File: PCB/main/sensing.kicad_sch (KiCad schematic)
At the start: 11 parts

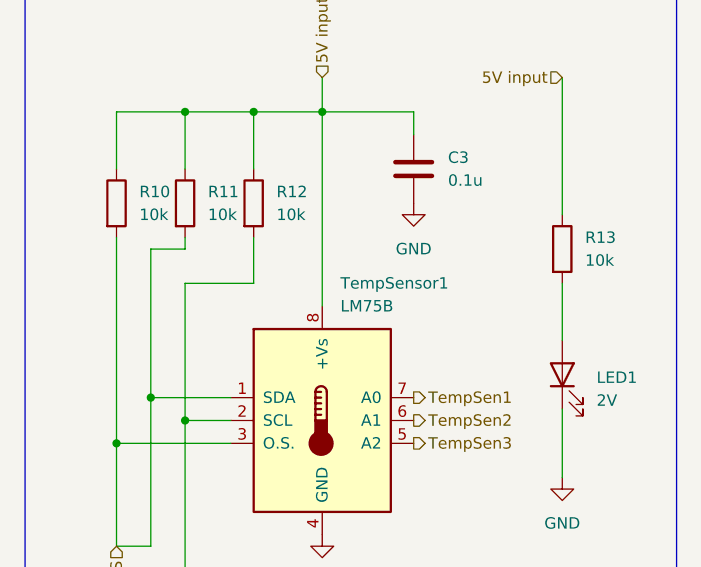
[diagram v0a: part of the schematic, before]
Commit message: rewired PCB and changed relevant footprints. production files regenerated
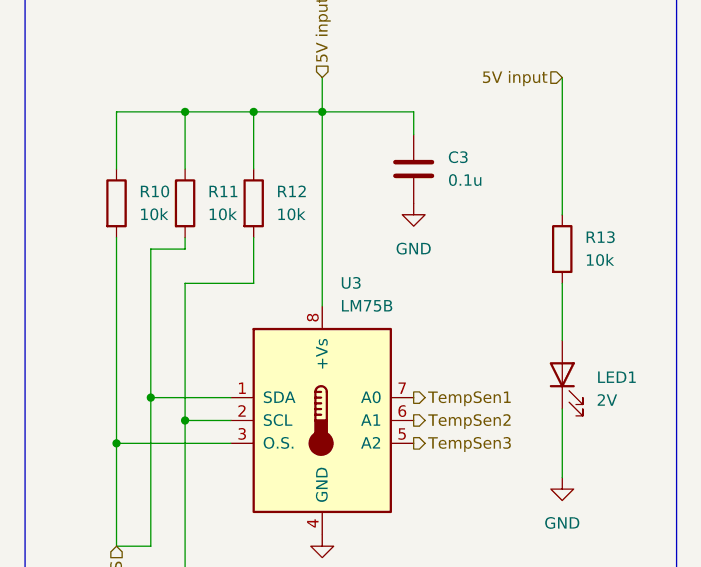
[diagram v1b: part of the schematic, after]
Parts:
- LDR1, LDR2: footprint Resistor_SMD:R_0201_0603Metric -> Resistor_THT:R_Axial_DIN0204_L3.6mm_D1.6mm_P1.90mm_Vertical
- R10, R11, R12, R13, R8, R9: footprint Resistor_SMD:R_0201_0603Metric -> Resistor_SMD:R_0603_1608Metric
- U3: renamed from TempSensor1; footprint Package_SO:MSOP-8_3x3mm_P0.65mm -> LM75BD:SOIC127P600X175-8N; LCSC C2837470 -> C34565; Price 0.4002 -> C34565
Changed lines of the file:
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@@
       (effects (font (size 1.27 1.27)) (justify left))
     )
-    (property "Footprint" "Resistor_SMD:R_0201_0603Metric" (id 2) (at 235.712 113.03 90)
+    (property "Footprint" "Resistor_SMD:R_0603_1608Metric" (id 2) (at 235.712 113.03 90)
       (effects (font (size 1.27 1.27)) hide)
     )
@@
       (effects (font (size 1.27 1.27)) (justify left))
     )
-    (property "Footprint" "Resistor_SMD:R_0201_0603Metric" (id 2) (at 153.67 99.06 0)
+    (property "Footprint" "Resistor_SMD:R_0603_1608Metric" (id 2) (at 153.67 99.06 0)
       (effects (font (size 1.27 1.27)) (justify left) hide)
     )
@@
       (effects (font (size 1.27 1.27)) (justify left))
     )
-    (property "Footprint" "Resistor_SMD:R_0201_0603Metric" (id 2) (at 220.472 113.03 90)
+    (property "Footprint" "Resistor_SMD:R_0603_1608Metric" (id 2) (at 220.472 113.03 90)
       (effects (font (size 1.27 1.27)) hide)
     )
@@
       (effects (font (size 1.27 1.27)) (justify left))
     )
-    (property "Footprint" "Resistor_SMD:R_0201_0603Metric" (id 2) (at 270.002 118.11 90)
+    (property "Footprint" "Resistor_SMD:R_0603_1608Metric" (id 2) (at 270.002 118.11 90)
       (effects (font (size 1.27 1.27)) hide)
     )
@@
       (effects (font (size 1.27 1.27)) (justify left))
     )
-    (property "Footprint" "Resistor_SMD:R_0201_0603Metric" (id 2) (at 128.27 140.97 90)
+    (property "Footprint" "Resistor_THT:R_Axial_DIN0204_L3.6mm_D1.6mm_P1.90mm_Vertical" (id 2) (at 128.27 140.97 90)
       (effects (font (size 1.27 1.27)) (justify left) hide)
     )
@@
       (effects (font (size 1.27 1.27)) (justify left))
     )
-    (property "Footprint" "Resistor_SMD:R_0201_0603Metric" (id 2) (at 100.33 105.41 0)
+    (property "Footprint" "Resistor_SMD:R_0603_1608Metric" (id 2) (at 100.33 105.41 0)
       (effects (font (size 1.27 1.27)) (justify left) hide)
     )
@@
       (effects (font (size 1.27 1.27)) (justify left))
     )
-    (property "Footprint" "Resistor_SMD:R_0201_0603Metric" (id 2) (at 228.092 113.03 90)
+    (property "Footprint" "Resistor_SMD:R_0603_1608Metric" (id 2) (at 228.092 113.03 90)
       (effects (font (size 1.27 1.27)) hide)
     )
@@
   (symbol (lib_id "Sensor_Temperature:LM75B") (at 245.11 137.16 0) (unit 1)
     (in_bom yes) (on_board yes) (fields_autoplaced)
-    (property "Reference" "TempSensor1" (id 0) (at 247.1294 121.92 0)
+    (property "Reference" "U3" (id 0) (at 247.1294 121.92 0)
       (effects (font (size 1.27 1.27)) (justify left))
     )
@@
       (effects (font (size 1.27 1.27)) (justify left))
     )
-    (property "Footprint" "Package_SO:MSOP-8_3x3mm_P0.65mm" (id 2) (at 245.11 137.16 0)
+    (property "Footprint" "LM75BD:SOIC127P600X175-8N" (id 2) (at 245.11 137.16 0)
       (effects (font (size 1.27 1.27)) hide)
     )
@@
       (effects (font (size 1.27 1.27)) hide)
     )
-    (property "LCSC" "C2837470" (id 4) (at 245.11 137.16 0)
-      (effects (font (size 1.27 1.27)) hide)
-    )
-    (property "Price" "0.4002" (id 5) (at 245.11 137.16 0)
+    (property "LCSC" "C34565" (id 4) (at 245.11 137.16 0)
+      (effects (font (size 1.27 1.27)) hide)
+    )
+    (property "Price" "C34565" (id 5) (at 245.11 137.16 0)
       (effects (font (size 1.27 1.27)) hide)
     )
@@
       (effects (font (size 1.27 1.27)) (justify left))
     )
-    (property "Footprint" "Resistor_SMD:R_0201_0603Metric" (id 2) (at 149.86 133.3499 0)
+    (property "Footprint" "Resistor_THT:R_Axial_DIN0204_L3.6mm_D1.6mm_P1.90mm_Vertical" (id 2) (at 149.86 133.3499 0)
       (effects (font (size 1.27 1.27)) (justify left) hide)
     )
